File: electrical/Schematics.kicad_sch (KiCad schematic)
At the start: 24 parts, among them J1 12V_IN, J2 RGB_STRIP_1, J3 WHITE_STRIP_1, J4 WHITE_STRIP_2, J5 RGB_STRIP_2, Q1 IRLB8721PBF, Q2 2N7000, Q3 IRLB8721PBF, Q4 2N7000, SW1 BTN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

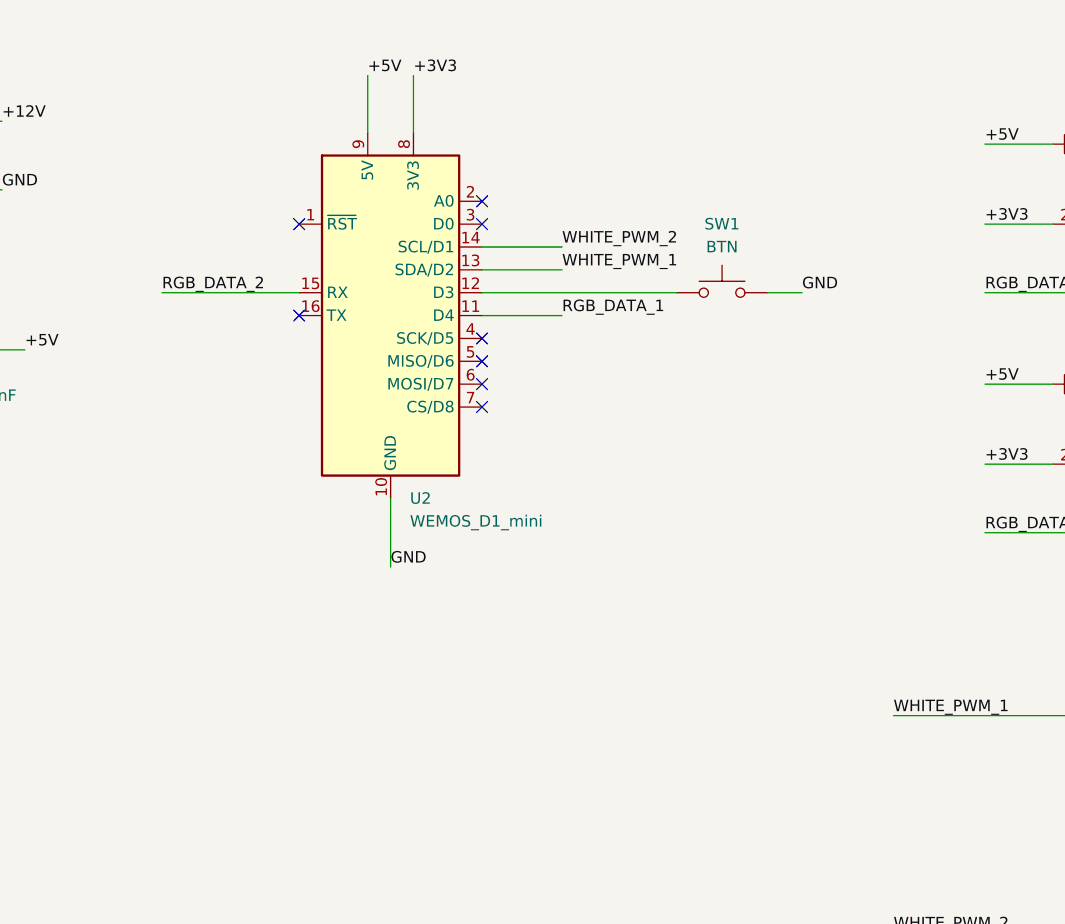
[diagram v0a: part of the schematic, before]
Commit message: changed design to fit the ordered esp module
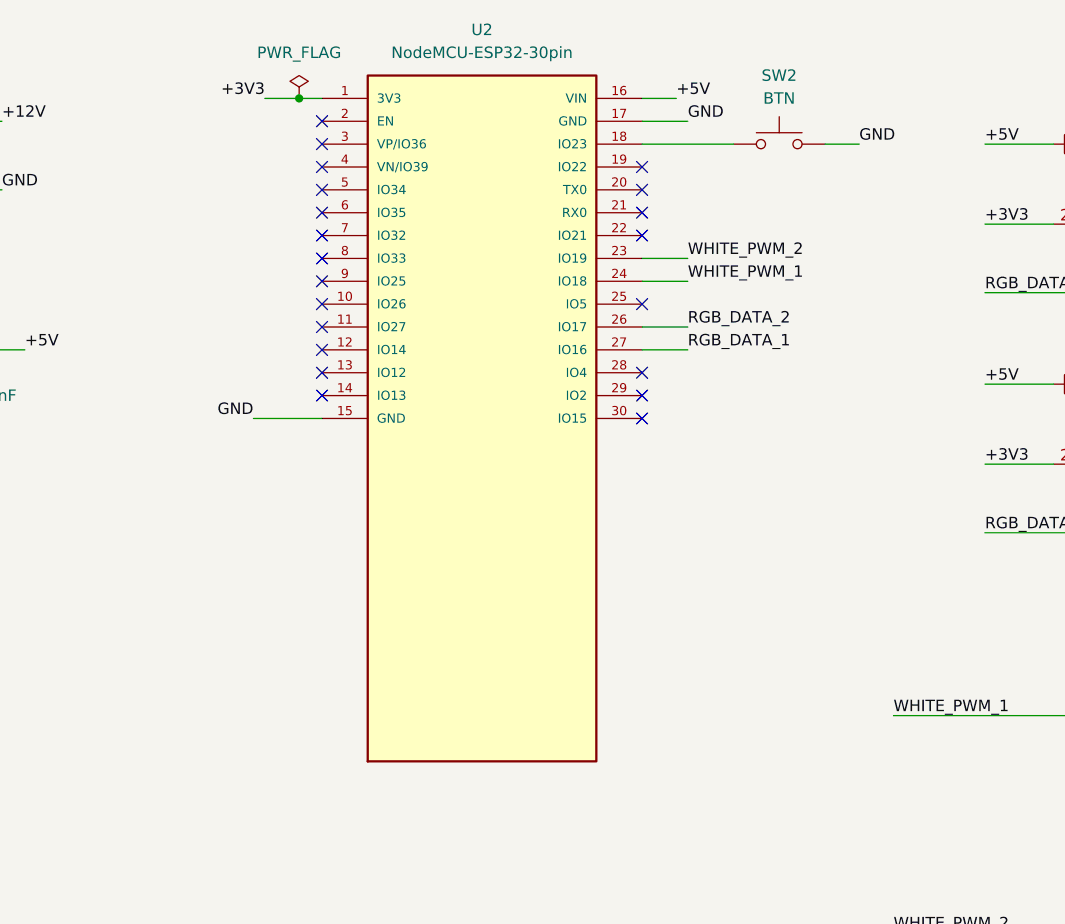
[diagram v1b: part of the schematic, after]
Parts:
- removed SW1: BTN, Button_Switch_THT:SW_PUSH_6mm, symbol Switch:SW_Push
- removed U2: WEMOS_D1_mini, RF_Module:WEMOS_D1_mini_light, symbol RF_Module:WEMOS_D1_mini
- added SW2: BTN, Button_Switch_THT:SW_PUSH_6mm, symbol Switch:SW_Push
- added U2: NodeMCU-ESP32-30pin, WideRangeLEDLamp:NodeMCU-ESP32-30pin, symbol WideRangeLEDLamp:NodeMCU-ESP32-30pin
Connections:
- net +3V3: now also U2.1 (3V3)
- net +5V: now also U2.16 (VIN)
- net GND: now also SW2.2, U2.15 (GND), U2.17 (GND)
- net RGB_DATA_1: now also U2.27 (IO16)
- net RGB_DATA_2: now also U2.26 (IO17)
- net WHITE_PWM_1: now also U2.24 (IO18)
- net WHITE_PWM_2: now also U2.23 (IO19)
- new net: SW2.1, U2.18 (IO23)
- no-connect marks 8 -> 21

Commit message: changes according to actual build
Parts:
- removed Q2, Q4: 2N7000, Package_TO_SOT_THT:TO-92_Inline, symbol Transistor_FET:2N7000
- removed R3, R7: R4K7, Resistor_THT:R_Axial_DIN0207_L6.3mm_D2.5mm_P10.16mm_Horizontal, symbol Device:R
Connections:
- net RGB_DATA_1: now also R4.1
- net RGB_DATA_2: now also R8.1
- net +3V3: no longer names the net of U2.1 (3V3)
- no-connect marks 21 -> 22
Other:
- moved on the sheet: R4, R8
